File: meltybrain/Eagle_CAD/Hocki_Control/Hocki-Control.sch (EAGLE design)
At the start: 146 parts, among them J1 SM03B-SRSS-TB(LF)(SN), J2 SM03B-SRSS-TB(LF)(SN), J3 SM03B-SRSS-TB(LF)(SN), J4 SM04B-SRSS-TB(LF)(SN), J5 SM04B-SRSS-TB(LF)(SN), J6 SM02B-SRSS-TB(LF)(SN), U1 TEENSY_4.1, U10 TLV3502AIDCNR, U11 NL27WZ32USG, U12 NL27WZ32USG, U13 HMC1052L-TR, U14 LMV358, U15 IRF7509, U16 TMUX1219DCKR, U17 LMV358, U18 LMV358, U19 AP2210K-3.3TRG1, U2 ADXL375, U20 AP2210K-5.0TRG1, U21 AP63200, U22 74AHC1G04GW,125, U23 LDL212PU50R, U3 ADXL375, U4 ADXL375, U5 ADXL375, U6 LMH6612MAX/NOPB, U7 LMH6612MAX/NOPB, U8 LMH6612MAX/NOPB, U9 LMH6612MAX/NOPB

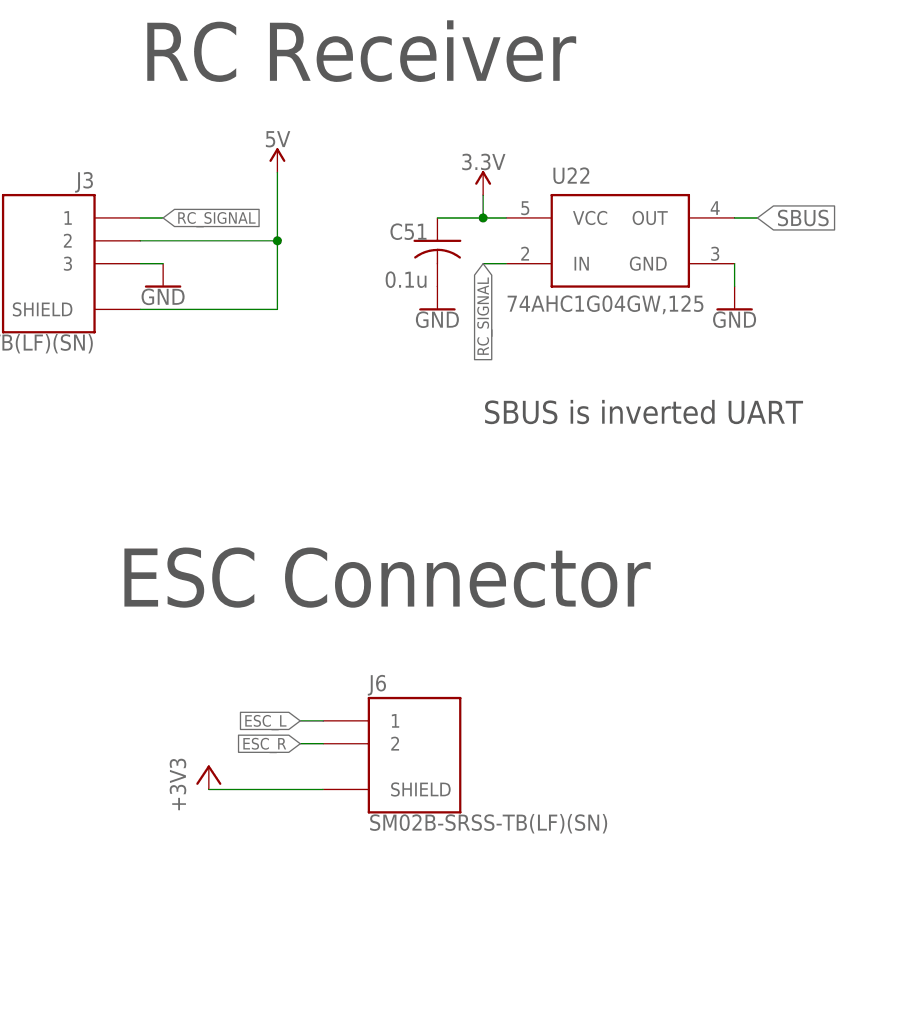
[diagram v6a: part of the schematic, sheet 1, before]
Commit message: control now 4 layers. silkscreen really needs work tho
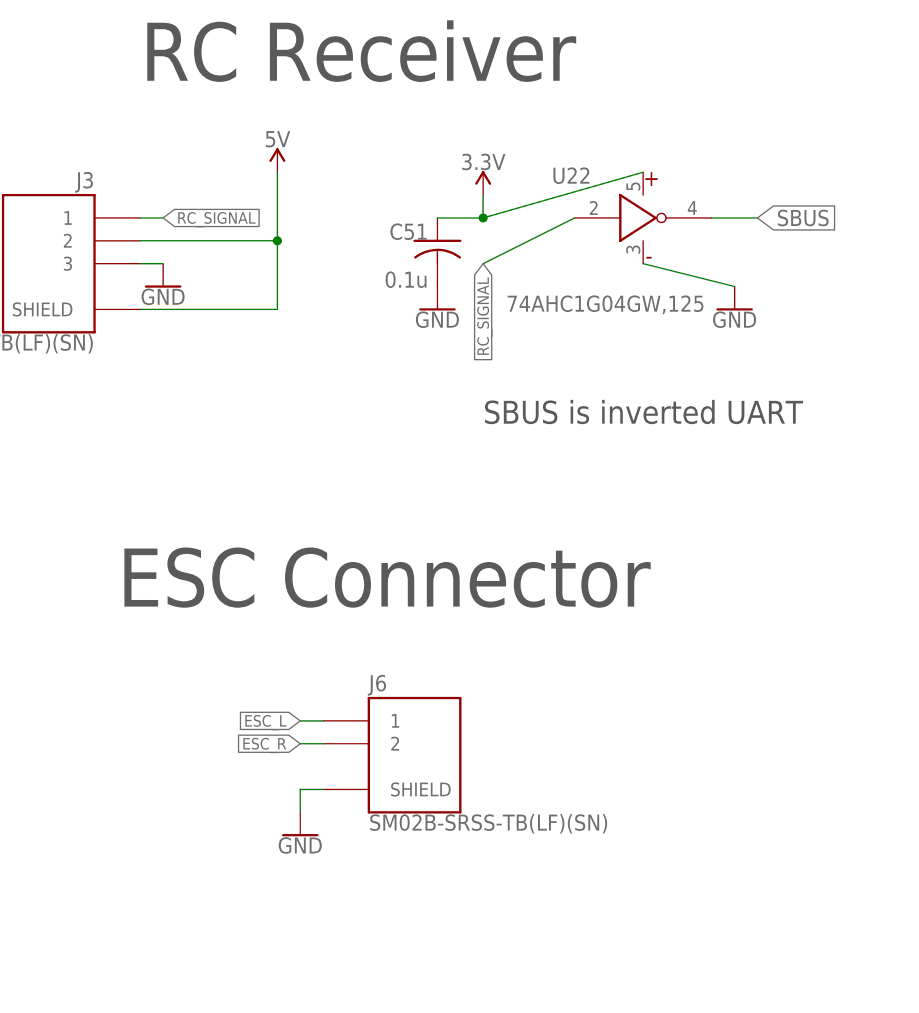
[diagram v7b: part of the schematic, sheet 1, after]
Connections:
- net +3V3: no longer J6.SHIELD
- net 5V: no longer J1.SHIELD, J2.SHIELD
- net GND: now also J1.SHIELD, J2.SHIELD, J6.SHIELD

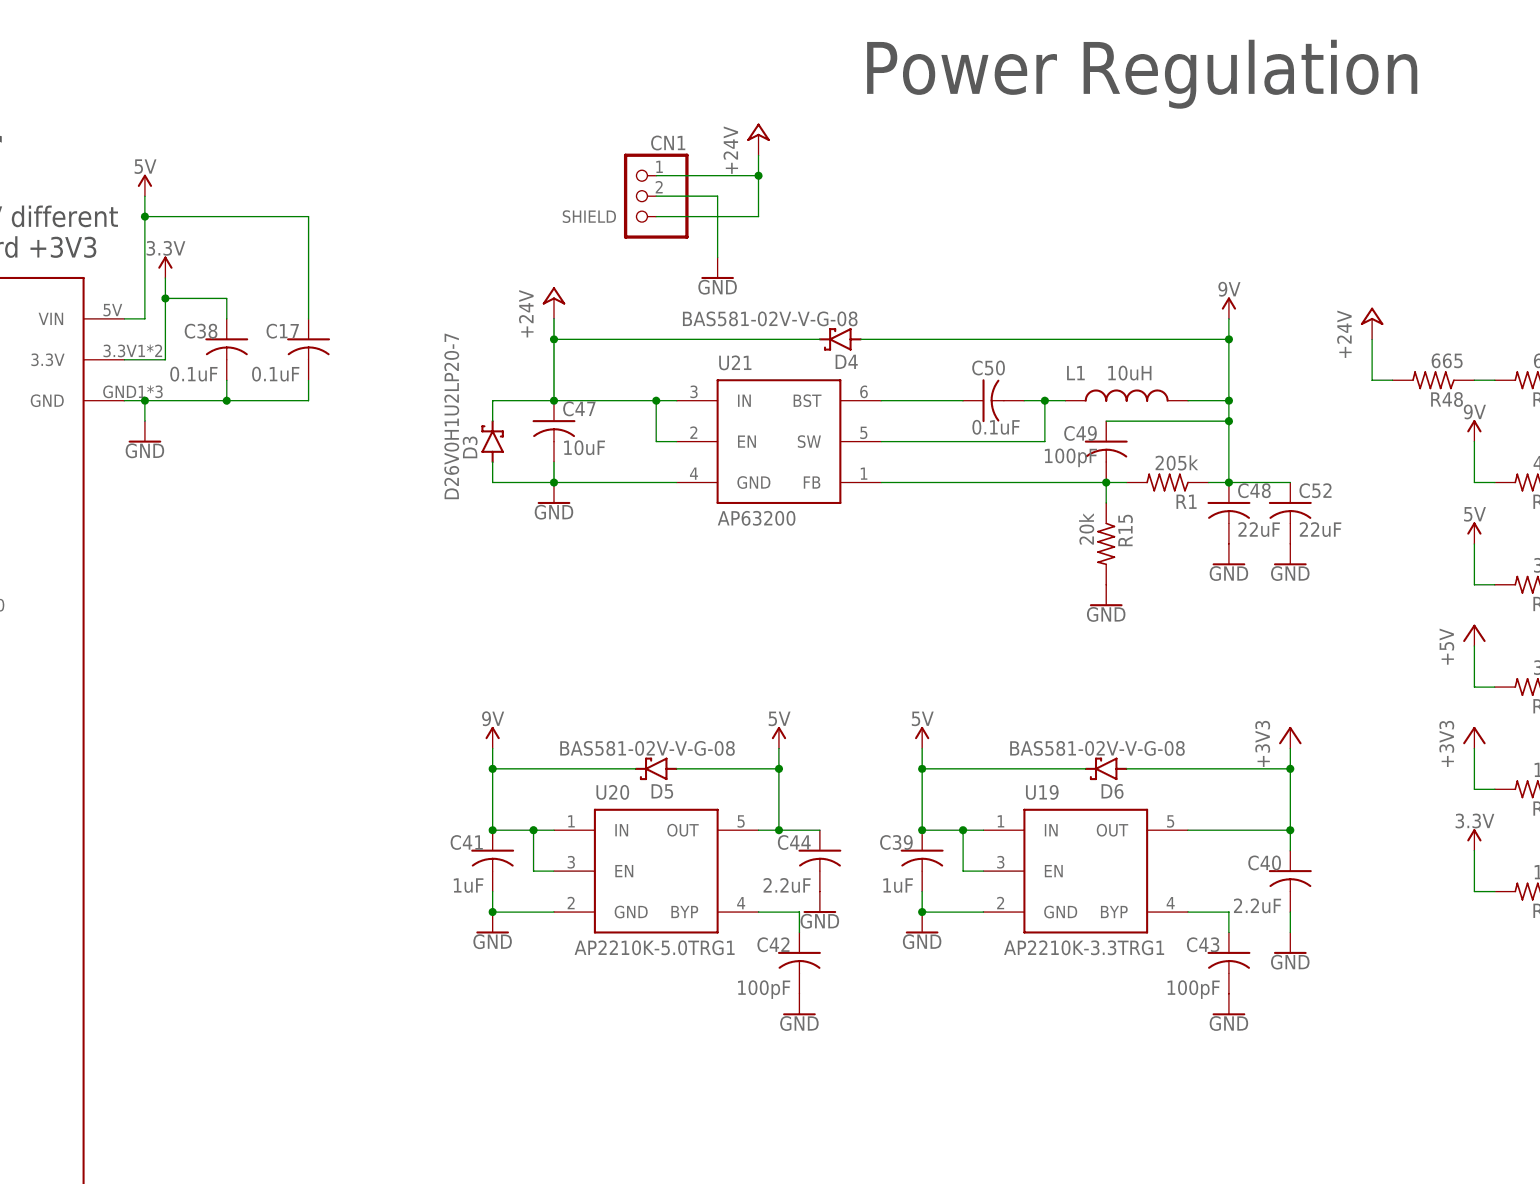
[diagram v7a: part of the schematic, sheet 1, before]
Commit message: added tvs diodes and did some silkscreen
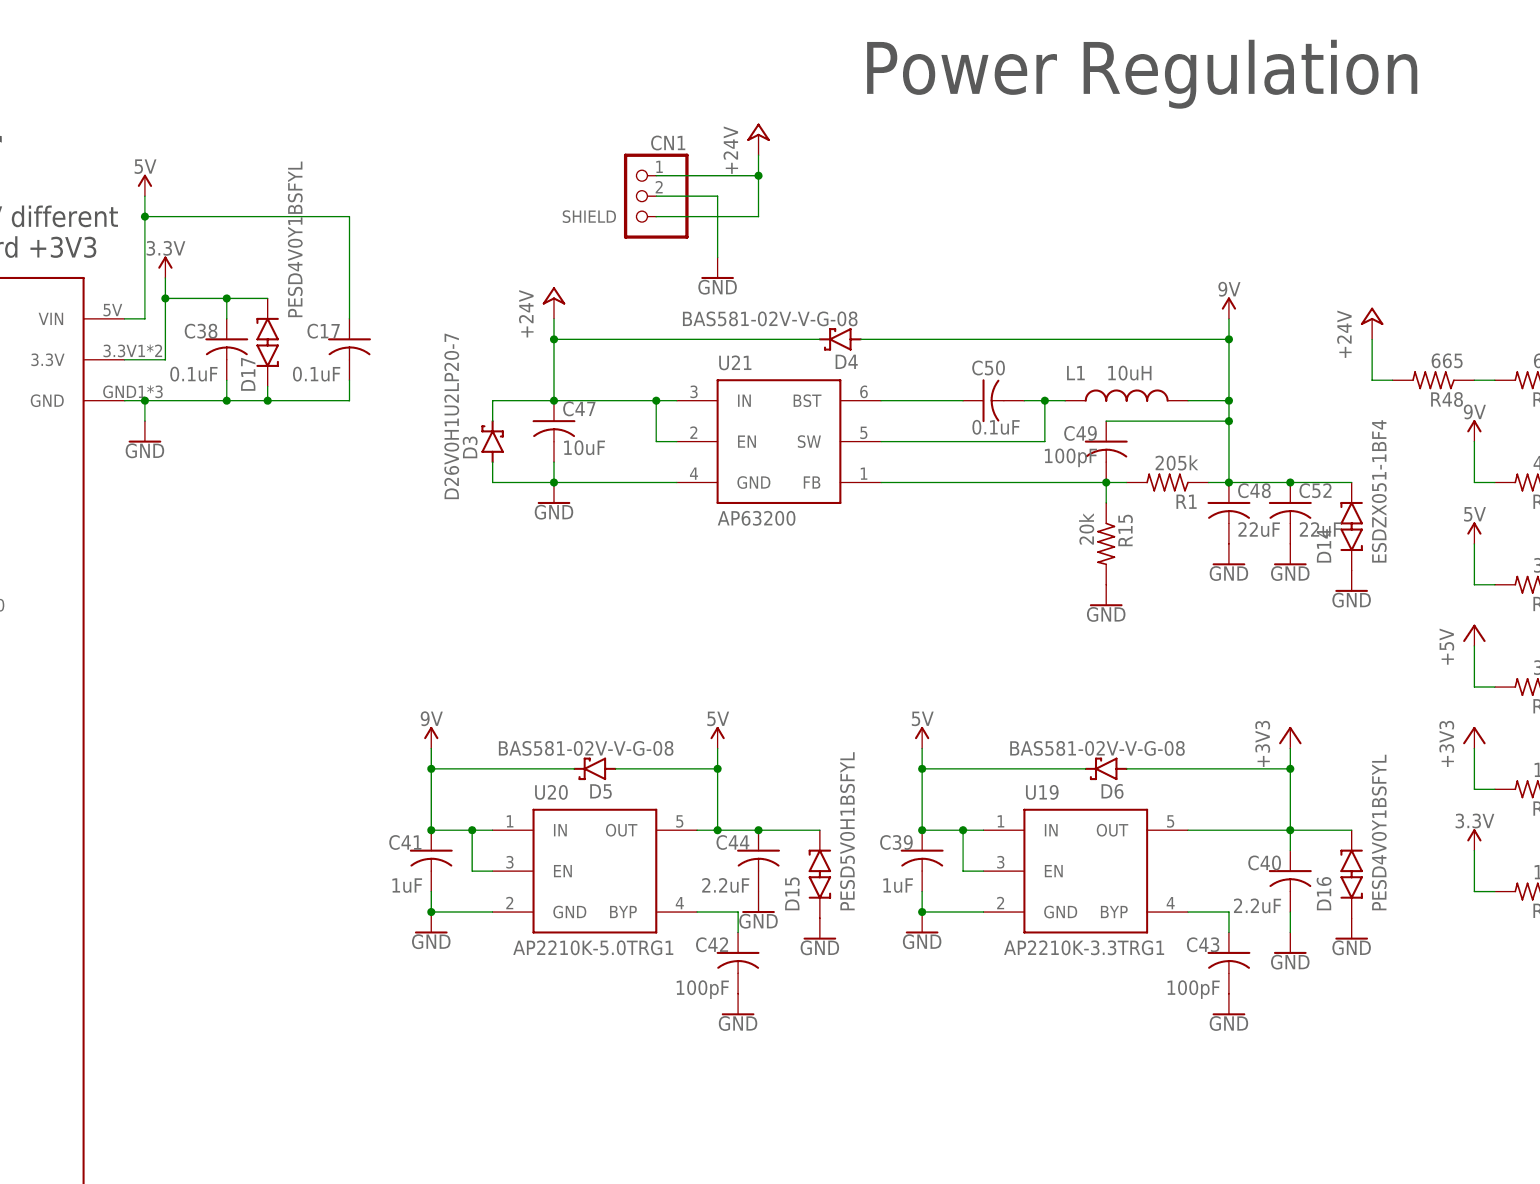
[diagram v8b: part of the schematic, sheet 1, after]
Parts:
- added D14: ESDZX051-1BF4, Hocki_Library:ESDZX051-1BF4
- added D15: PESD5V0H1BSFYL, Hocki_Library:PESD5V0H1BSFYL
- added D16, D17: PESD4V0Y1BSFYL, Hocki_Library:PESD4V0Y1BSFYL
- C10: value 1u -> 1uF
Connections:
- net +3V3: now also D16.C2
- net 3.3V: now also D17.C2
- net 5V: now also D15.C2
- net 9V: now also D14.C2
- net GND: now also D14.C1, D15.C1, D16.C1, D17.C1
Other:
- moved on the sheet: C17, C41, C42, C44, D5, U20
